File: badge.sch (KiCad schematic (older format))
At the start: 41 parts, among them U1 TPS61165

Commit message: Make extension half pmod, and left one led, added battery switch.
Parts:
- removed D?: GREEN LED, symbol LED
- removed J?: Conn_01x03, symbol Conn_01x03
- removed R?: 330, symbol R
- added J?: Conn_01x06, symbol Conn_01x06
- added SW?: SW_SPDT, symbol SW_SPDT
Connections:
- net labels added: EXT3, LED
- net labels removed: LED0, LED1, LED_0, LED_1
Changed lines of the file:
@@
 EXT2
 Text Label 7900 5200 0    60   ~ 0
-LED0
+EXT3
 Text Label 7900 5300 0    60   ~ 0
-LED1
+LED
 Text Label 7900 5400 0    60   ~ 0
 OSC_OUT
@@
 $EndComp
 $Comp
-L LED D?
-U 1 1 5A7FC7EE
-P 9600 7400
-F 0 "D?" H 9600 7500 50  0000 C CNN
-F 1 "GREEN LED" H 9600 7300 50  0000 C CNN
-F 2 "" H 9600 7400 50  0001 C CNN
-F 3 "" H 9600 7400 50  0001 C CNN
-	1    9600 7400
-	1    0    0    -1
-$EndComp
-$Comp
 L R R?
 U 1 1 5A7FC9C8
@@
 	0    1    1    0
 $EndComp
-$Comp
-L R R?
-U 1 1 5A7FCA37
-P 10000 7400
-F 0 "R?" V 10080 7400 50  0000 C CNN
-F 1 "330" V 10000 7400 50  0000 C CNN
-F 2 "" V 9930 7400 50  0001 C CNN
-F 3 "" H 10000 7400 50  0001 C CNN
-	1    10000 7400
-	0    1    1    0
-$EndComp
 Text Label 10300 7100 0    60   ~ 0
-LED_0
-Text Label 10300 7400 0    60   ~ 0
-LED_1
+LED
 $Comp
 L GND #PWR?
 U 1 1 5A7FCB50
-P 9250 7600
-F 0 "#PWR?" H 9250 7350 50  0001 C CNN
-F 1 "GND" H 9250 7450 50  0000 C CNN
-F 2 "" H 9250 7600 50  0001 C CNN
-F 3 "" H 9250 7600 50  0001 C CNN
-	1    9250 7600
-	1    0    0    -1
+P 9250 7100
+F 0 "#PWR?" H 9250 6850 50  0001 C CNN
+F 1 "GND" H 9250 6950 50  0000 C CNN
+F 2 "" H 9250 7100 50  0001 C CNN
+F 3 "" H 9250 7100 50  0001 C CNN
+	1    9250 7100
+	0    1    1    0
 $EndComp
 Wire Wire Line
@@
 	9450 7100 9250 7100
 Wire Wire Line
-	9250 7100 9250 7600
-Wire Wire Line
-	9450 7400 9250 7400
-Connection ~ 9250 7400
-Wire Wire Line
 	10300 7100 10150 7100
 Wire Wire Line
 	9850 7100 9750 7100
-Wire Wire Line
-	10300 7400 10100 7400
-Wire Wire Line
-	9850 7400 9750 7400
-$Comp
-L Conn_01x03 J?
-U 1 1 5A7FE0A3
-P 8700 7500
-F 0 "J?" H 8700 7700 50  0000 C CNN
-F 1 "Conn_01x03" H 8700 7300 50  0000 C CNN
-F 2 "" H 8700 7500 50  0001 C CNN
-F 3 "" H 8700 7500 50  0001 C CNN
-	1    8700 7500
-	1    0    0    -1
-$EndComp
 $Comp
 L Conn_01x02 BATTERY
@@
 L +3.3V #PWR?
 U 1 1 5A8061E0
-P 6850 3500
-F 0 "#PWR?" H 6850 3350 50  0001 C CNN
-F 1 "+3.3V" H 6850 3640 50  0000 C CNN
-F 2 "" H 6850 3500 50  0001 C CNN
-F 3 "" H 6850 3500 50  0001 C CNN
-	1    6850 3500
+P 6750 3600
+F 0 "#PWR?" H 6750 3450 50  0001 C CNN
+F 1 "+3.3V" H 6750 3740 50  0000 C CNN
+F 2 "" H 6750 3600 50  0001 C CNN
+F 3 "" H 6750 3600 50  0001 C CNN
+	1    6750 3600
 	0    -1   -1   0
 $EndComp
 Wire Wire Line
 	7050 3400 7450 3400
-Wire Wire Line
-	6850 3500 7450 3500
+$Comp
+L SW_SPDT SW?
+U 1 1 5A7F0442
+P 7050 3600
+F 0 "SW?" H 7050 3770 50  0000 C CNN
+F 1 "SW_SPDT" H 7050 3400 50  0000 C CNN
+F 2 "" H 7050 3600 50  0001 C CNN
+F 3 "" H 7050 3600 50  0001 C CNN
+	1    7050 3600
+	1    0    0    -1
+$EndComp
+Wire Wire Line
+	7250 3500 7450 3500
+Wire Wire Line
+	6750 3600 6850 3600
+Text Label 8150 7700 0    60   ~ 0
+EXT3
+Wire Wire Line
+	8150 7700 8500 7700
+$Comp
+L Conn_01x06 J?
+U 1 1 5A7F0509
+P 8700 7600
+F 0 "J?" H 8700 7900 50  0000 C CNN
+F 1 "Conn_01x06" H 8700 7200 50  0000 C CNN
+F 2 "" H 8700 7600 50  0001 C CNN
+F 3 "" H 8700 7600 50  0001 C CNN
+	1    8700 7600
+	1    0    0    -1
+$EndComp
+$Comp
+L GND #PWR?
+U 1 1 5A7F0582
+P 8300 7800
+F 0 "#PWR?" H 8300 7550 50  0001 C CNN
+F 1 "GND" H 8300 7650 50  0000 C CNN
+F 2 "" H 8300 7800 50  0001 C CNN
+F 3 "" H 8300 7800 50  0001 C CNN
+	1    8300 7800
+	0    1    1    0
+$EndComp
+$Comp
+L +3.3V #PWR?
+U 1 1 5A7F0636
+P 8300 7900
+F 0 "#PWR?" H 8300 7750 50  0001 C CNN
+F 1 "+3.3V" H 8300 8040 50  0000 C CNN
+F 2 "" H 8300 7900 50  0001 C CNN
+F 3 "" H 8300 7900 50  0001 C CNN
+	1    8300 7900
+	0    -1   -1   0
+$EndComp
+Wire Wire Line
+	8300 7800 8500 7800
+Wire Wire Line
+	8300 7900 8500 7900
 $EndSCHEMATC

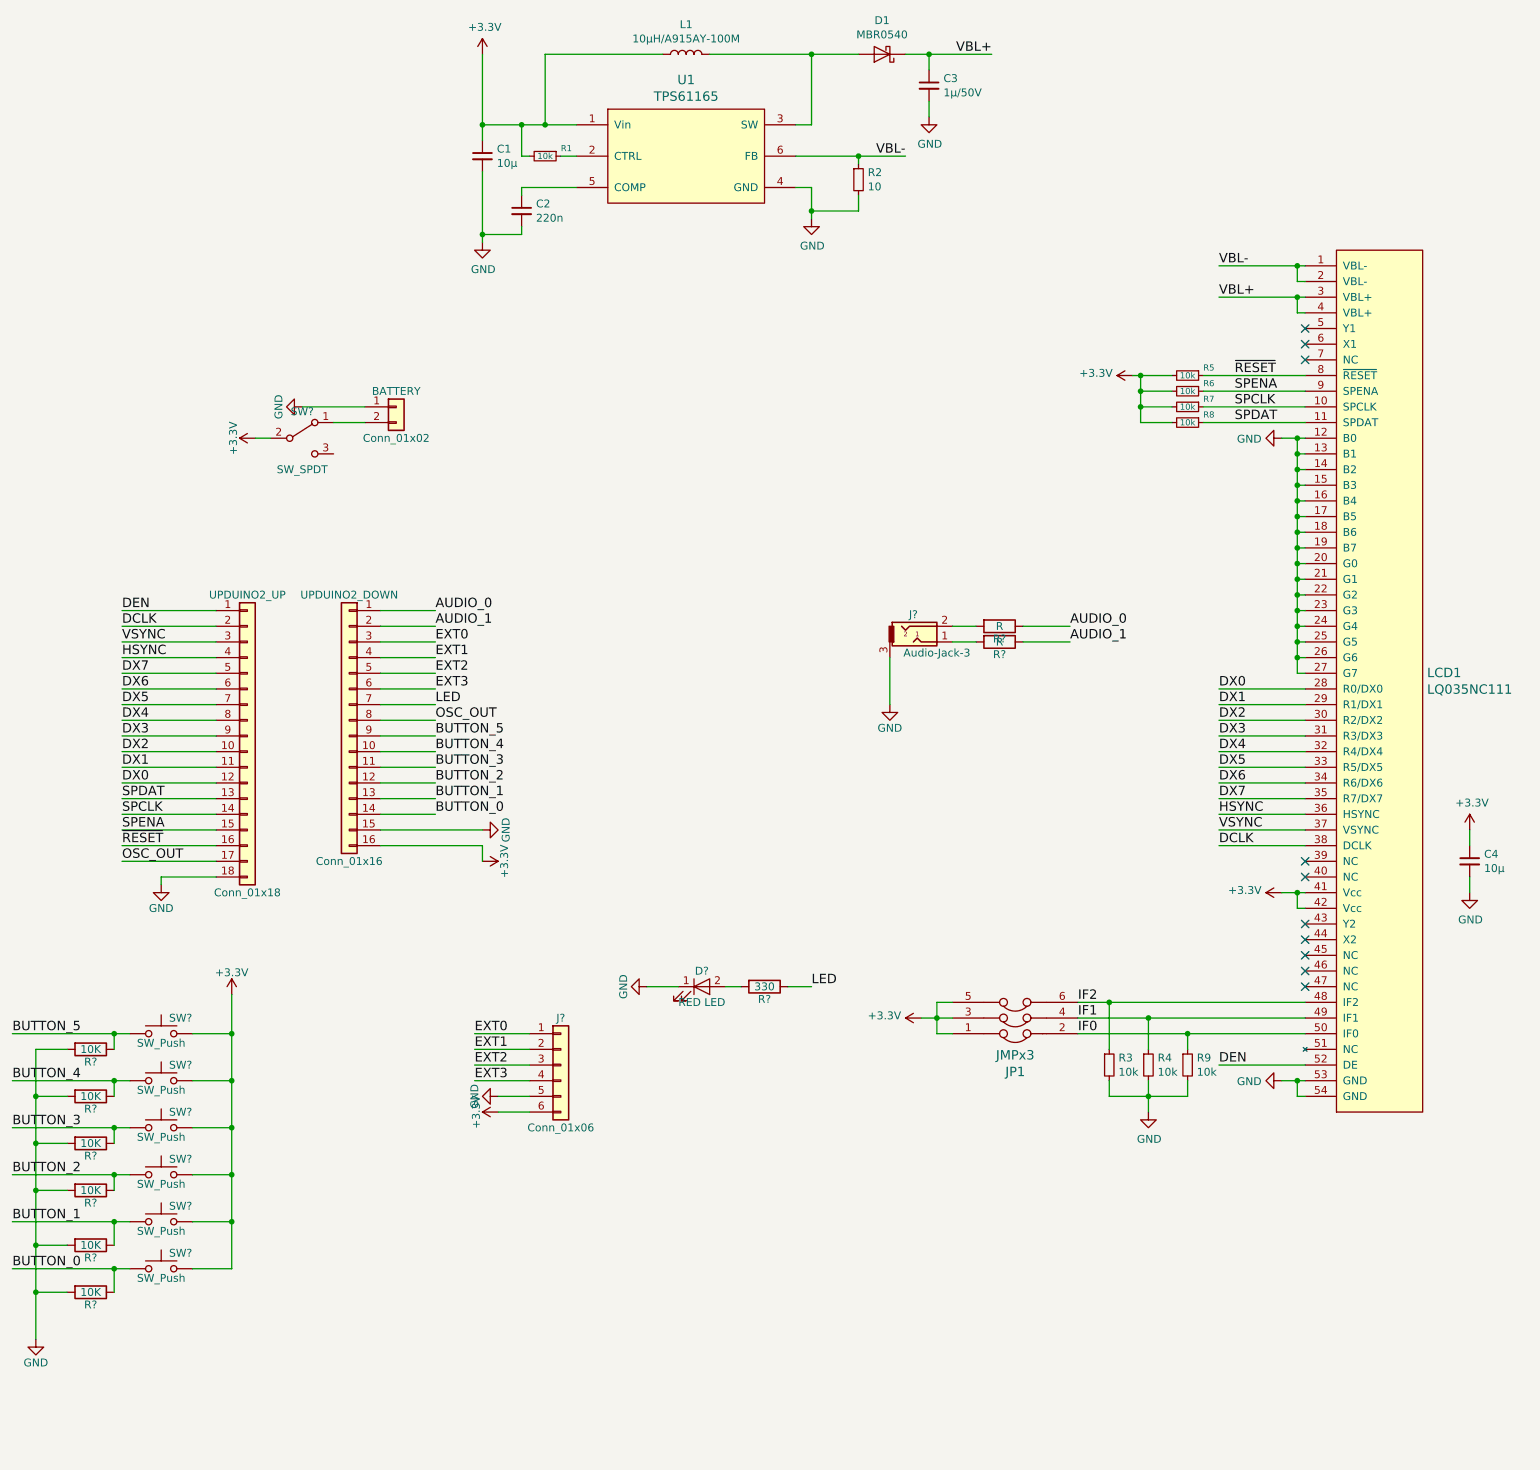
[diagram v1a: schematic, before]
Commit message: removed SPI on LED to optimize, drive TPS control, 2 leds on dedicated PLL ports
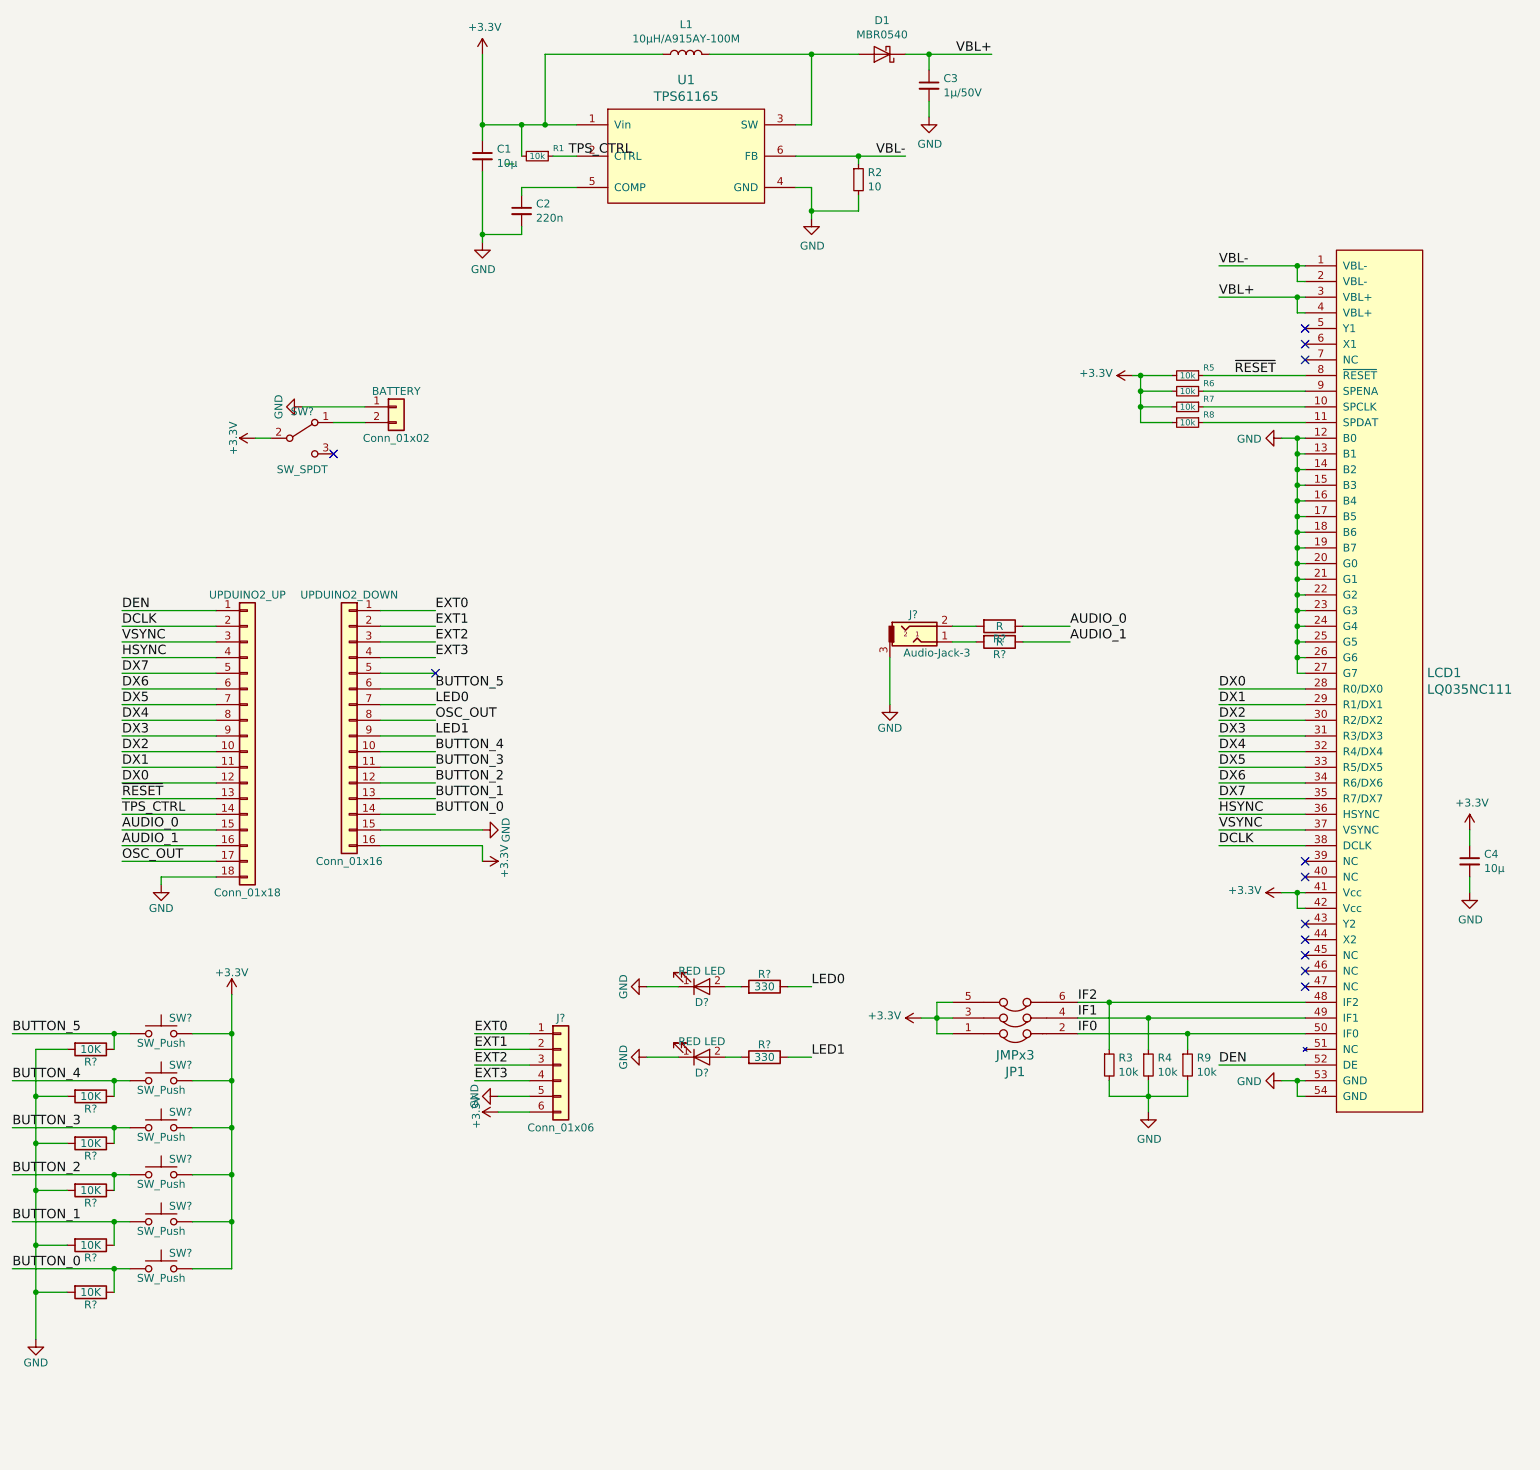
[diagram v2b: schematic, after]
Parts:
- added D?: RED LED, symbol LED
- added R?: 330, symbol R
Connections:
- net AUDIO_0: now also UPDUINO2_UP.15 (Pin_15); no longer UPDUINO2_DOWN.1 (Pin_1)
- net AUDIO_1: now also UPDUINO2_UP.16 (Pin_16); no longer UPDUINO2_DOWN.2 (Pin_2)
- net BUTTON_5: now also UPDUINO2_DOWN.6 (Pin_6); no longer UPDUINO2_DOWN.9 (Pin_9)
- net EXT0: now also UPDUINO2_DOWN.1 (Pin_1); no longer UPDUINO2_DOWN.3 (Pin_3)
- net EXT1: now also UPDUINO2_DOWN.2 (Pin_2); no longer UPDUINO2_DOWN.4 (Pin_4)
- net EXT2: now also UPDUINO2_DOWN.3 (Pin_3); no longer UPDUINO2_DOWN.5 (Pin_5)
- net EXT3: now also UPDUINO2_DOWN.4 (Pin_4); no longer UPDUINO2_DOWN.6 (Pin_6)
- net GND: now also D?.1 (K)
- net ~RESET: now also UPDUINO2_UP.13 (Pin_13); no longer UPDUINO2_UP.16 (Pin_16)
- net TPS_CTRL: now reaches R1.1, U1.2 (CTRL)
- net TPS_CTRL: now also UPDUINO2_UP.14 (Pin_14)
- net LED renamed LED0
- net SPCLK: no longer names the net of LCD1.10 (SPCLK), R7.1
- net SPCLK: no longer UPDUINO2_UP.14 (Pin_14)
- net SPDAT: no longer names the net of LCD1.11 (SPDAT), R8.1
- net SPDAT: no longer UPDUINO2_UP.13 (Pin_13)
- net SPENA: no longer names the net of LCD1.9 (SPENA), R6.1
- net SPENA: no longer UPDUINO2_UP.15 (Pin_15)
- new net: D?.2 (A), R?.2
- new net LED1: R?.1, UPDUINO2_DOWN.9 (Pin_9)
- no-connect marks 10 -> 12
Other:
- moved on the sheet: R1
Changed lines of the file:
@@
 encoding utf-8
 Sheet 1 1
-Title ""
+Title "FPGA Workshop Badge for Hackaday Belgrade 2018"
 Date ""
-Rev ""
-Comp ""
+Rev "1.0"
+Comp "David Shah and Miodrag Milanovic"
 Comment1 ""
 Comment2 ""
@@
 	0    1    1    0
 $EndComp
-Text Label 13000 3300 0    60   ~ 0
-SPENA
 $Comp
 L R_Small R6
@@
 	0    1    1    0
 $EndComp
-Text Label 13000 3400 0    60   ~ 0
-SPCLK
-Text Label 13000 3500 0    60   ~ 0
-SPDAT
 Text Label 12900 6000 0    60   ~ 0
 HSYNC
@@
 L R_Small R1
 U 1 1 5A4ACF50
-P 8600 1800
-F 0 "R1" V 8550 1900 39  0000 L CNN
-F 1 "10k" V 8600 1800 39  0000 C CNN
-F 2 "Resistors_SMD:R_0603" H 8600 1800 50  0001 C CNN
-F 3 "" H 8600 1800 50  0001 C CNN
-	1    8600 1800
+P 8550 1800
+F 0 "R1" V 8500 1900 39  0000 L CNN
+F 1 "10k" V 8550 1800 39  0000 C CNN
+F 2 "Resistors_SMD:R_0603" H 8550 1800 50  0001 C CNN
+F 3 "" H 8550 1800 50  0001 C CNN
+	1    8550 1800
 	0    1    1    0
 $EndComp
@@
 DEN
 Text Label 5900 6200 0    60   ~ 0
+AUDIO_1
+Text Label 5900 6100 0    60   ~ 0
+AUDIO_0
+Text Label 5900 6000 0    60   ~ 0
+TPS_CTRL
+Text Label 5900 5900 0    60   ~ 0
 ~RESET
-Text Label 5900 6100 0    60   ~ 0
-SPENA
-Text Label 5900 6000 0    60   ~ 0
-SPCLK
-Text Label 5900 5900 0    60   ~ 0
-SPDAT
 $Comp
 L GND #PWR?
@@
 AUDIO_0
 Text Label 7900 4700 0    60   ~ 0
-AUDIO_0
+EXT0
 Text Label 7900 4800 0    60   ~ 0
-AUDIO_1
+EXT1
 Text Label 11950 4900 0    60   ~ 0
 AUDIO_1
@@
 Text Label 7900 5600 0    60   ~ 0
 BUTTON_4
-Text Label 7900 5500 0    60   ~ 0
-BUTTON_5
 $Comp
 L SW_Push SW?
@@
 EXT2
 Text Label 7900 4900 0    60   ~ 0
-EXT0
+EXT2
 Text Label 7900 5000 0    60   ~ 0
-EXT1
-Text Label 7900 5100 0    60   ~ 0
-EXT2
+EXT3
 Text Label 7900 5200 0    60   ~ 0
-EXT3
-Text Label 7900 5300 0    60   ~ 0
-LED
+BUTTON_5
 Text Label 7900 5400 0    60   ~ 0
 OSC_OUT
@@
 F 3 "" H 9600 7100 50  0001 C CNN
 	1    9600 7100
-	1    0    0    -1
+	1    0    0    1
 $EndComp
 $Comp
@@
 F 3 "" H 10000 7100 50  0001 C CNN
 	1    10000 7100
-	0    1    1    0
+	0    1    -1   0
 $EndComp
 Text Label 10300 7100 0    60   ~ 0
-LED
+LED0
 $Comp
 L GND #PWR?
@@
 F 3 "" H 9250 7100 50  0001 C CNN
 	1    9250 7100
-	0    1    1    0
+	0    1    -1   0
 $EndComp
 Wire Wire Line
@@
 Wire Wire Line
 	7550 5400 7900 5400
-Wire Wire Line
-	7550 5300 7900 5300
 Wire Wire Line
 	7550 5200 7900 5200
@@
 Wire Wire Line
 	12800 3200 13450 3200
-Wire Wire Line
-	12800 3500 13450 3500
-Wire Wire Line
-	13450 3400 12800 3400
-Wire Wire Line
-	12800 3300 13450 3300
 Wire Wire Line
 	12400 3500 12600 3500
@@
 	8450 2000 8800 2000
 Wire Wire Line
-	8700 1800 8800 1800
-Wire Wire Line
-	8500 1800 8450 1800
-Wire Wire Line
-	8450 1800 8450 1600
-Connection ~ 8450 1600
+	8400 1850 8350 1850
 Wire Wire Line
 	10200 1600 10300 1600
@@
 Wire Wire Line
 	7900 5600 7550 5600
-Wire Wire Line
-	7900 5500 7550 5500
 Wire Wire Line
 	6350 7700 6600 7700
@@
 Wire Wire Line
 	8300 7900 8500 7900
+Wire Wire Line
+	13450 3300 12800 3300
+Wire Wire Line
+	13450 3400 12800 3400
+Wire Wire Line
+	13450 3500 12800 3500
+Text Label 7900 5300 0    60   ~ 0
+LED0
+Text Label 7900 5500 0    60   ~ 0
+LED1
+Wire Wire Line
+	7900 5300 7550 5300
+Wire Wire Line
+	7900 5500 7550 5500
+$Comp
+L LED D?
+U 1 1 5A7F8496
+P 9600 7550
+F 0 "D?" H 9600 7650 50  0000 C CNN
+F 1 "RED LED" H 9600 7450 50  0000 C CNN
+F 2 "" H 9600 7550 50  0001 C CNN
+F 3 "" H 9600 7550 50  0001 C CNN
+	1    9600 7550
+	1    0    0    1
+$EndComp
+$Comp
+L R R?
+U 1 1 5A7F849C
+P 10000 7550
+F 0 "R?" V 10080 7550 50  0000 C CNN
+F 1 "330" V 10000 7550 50  0000 C CNN
+F 2 "" V 9930 7550 50  0001 C CNN
+F 3 "" H 10000 7550 50  0001 C CNN
+	1    10000 7550
+	0    1    -1   0
+$EndComp
+Text Label 10300 7550 0    60   ~ 0
+LED1
+$Comp
+L GND #PWR?
+U 1 1 5A7F84A3
+P 9250 7550
+F 0 "#PWR?" H 9250 7300 50  0001 C CNN
+F 1 "GND" H 9250 7400 50  0000 C CNN
+F 2 "" H 9250 7550 50  0001 C CNN
+F 3 "" H 9250 7550 50  0001 C CNN
+	1    9250 7550
+	0    1    -1   0
+$EndComp
+Wire Wire Line
+	9450 7550 9250 7550
+Wire Wire Line
+	10300 7550 10150 7550
+Wire Wire Line
+	9850 7550 9750 7550
+Text Label 8750 1800 0    60   ~ 0
+TPS_CTRL
+Wire Wire Line
+	8650 1800 8800 1800
+Wire Wire Line
+	8450 1800 8450 1600
+Connection ~ 8450 1600
+NoConn ~ 7900 5100
+NoConn ~ 7250 3700
 $EndSCHEMATC
